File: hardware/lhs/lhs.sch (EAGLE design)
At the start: 21 parts, among them IC1 MCP23017SP

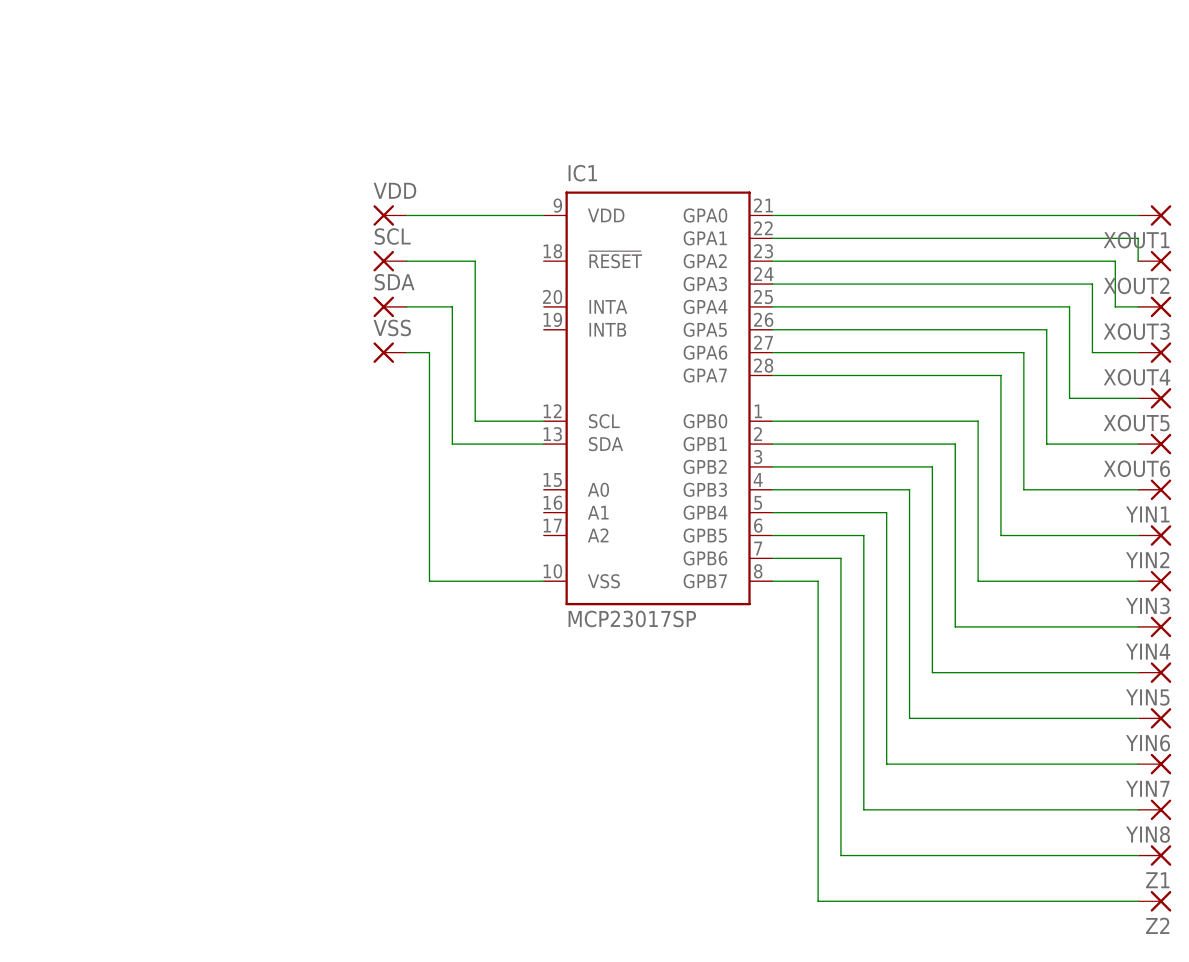
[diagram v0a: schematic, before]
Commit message: Added multiplexer design
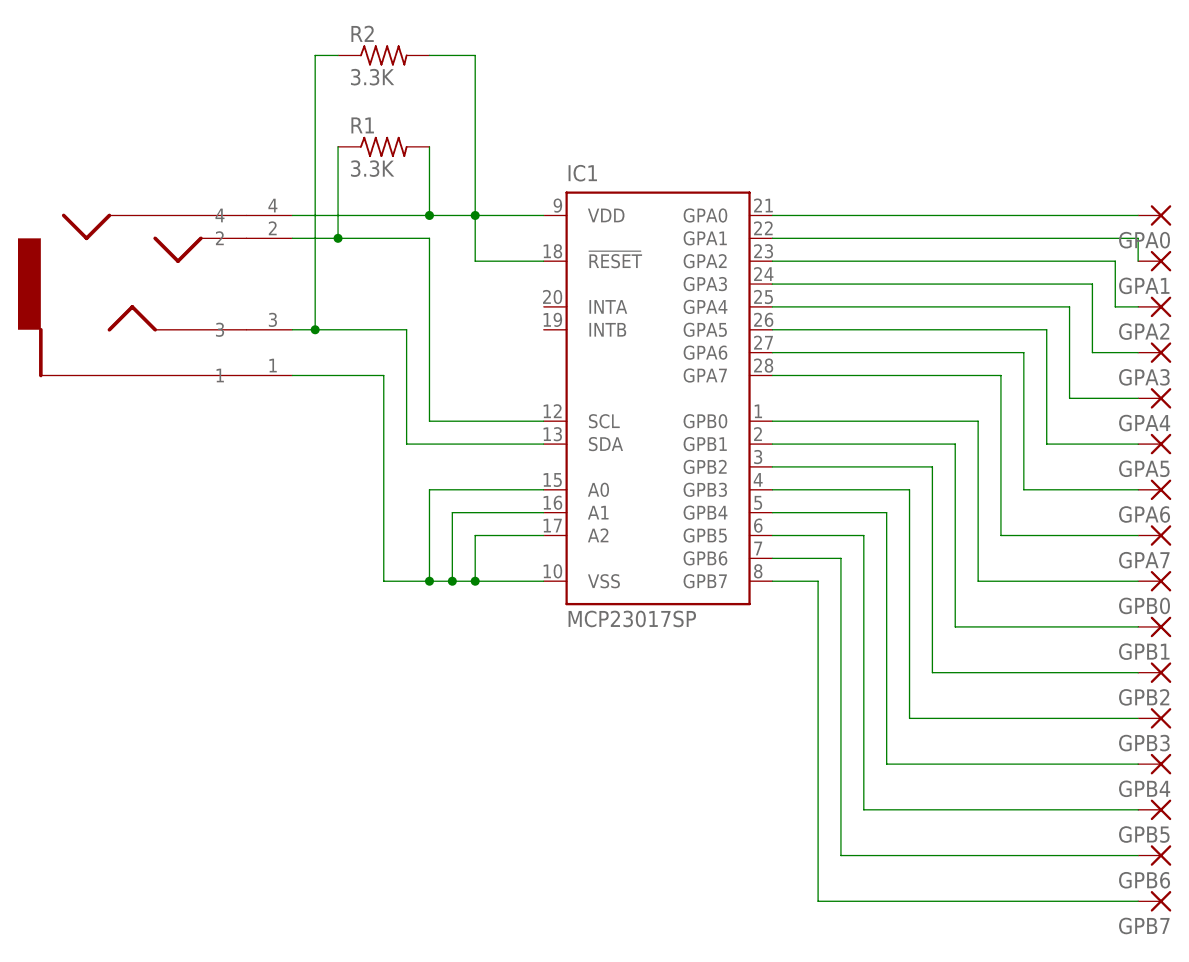
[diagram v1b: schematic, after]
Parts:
- removed SCL, SDA, VDD, VSS: (no value), wirepad:1,6/0,8
- added R1, R2: 3.3K, adafruit:R-US_0207/10
- added U$1: SJ-43514_HEADPHONES_3.5MM_X4, my_parts:SJ-43514_HEADPHONES_3.5MM_X4
- renumbered XOUT1 to GPA0, XOUT2 to GPA1, XOUT3 to GPA2, XOUT4 to GPA3, XOUT5 to GPA4, XOUT6 to GPA5, YIN1 to GPA6, YIN2 to GPA7, YIN3 to GPB0, YIN4 to GPB1, YIN5 to GPB2, YIN6 to GPB3, YIN7 to GPB4, YIN8 to GPB5, Z1 to GPB6, Z2 to GPB7
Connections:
- net N$1: now also IC1.!RESET, R1.2, R2.2, U$1.4; no longer VDD.P
- net N$2: now also IC1.A0, IC1.A1, IC1.A2, U$1.1; no longer VSS.P
- net N$3: now also R1.1, U$1.2; no longer SCL.P
- net N$4: now also R2.1, U$1.3; no longer SDA.P
